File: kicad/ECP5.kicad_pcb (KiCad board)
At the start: 4 copper layers, 64.4 x 54.6 mm, 28 parts, among them J1 FLE-126-01-G-DV, SW1 PTS645SK43SMTR92 LFS

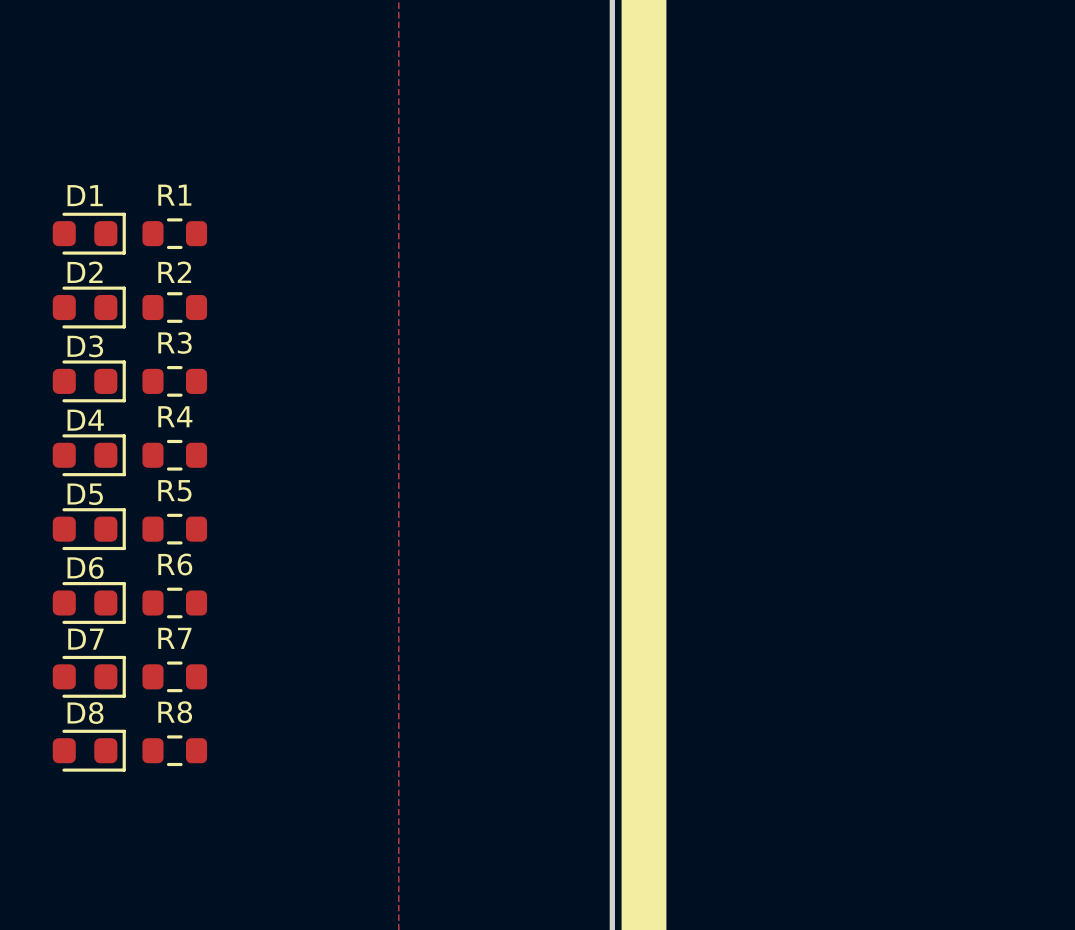
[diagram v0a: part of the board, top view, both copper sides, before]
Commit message: Changed the name of the project path to ECP5_BGA381_FT2232HQ_FIFO_EXT
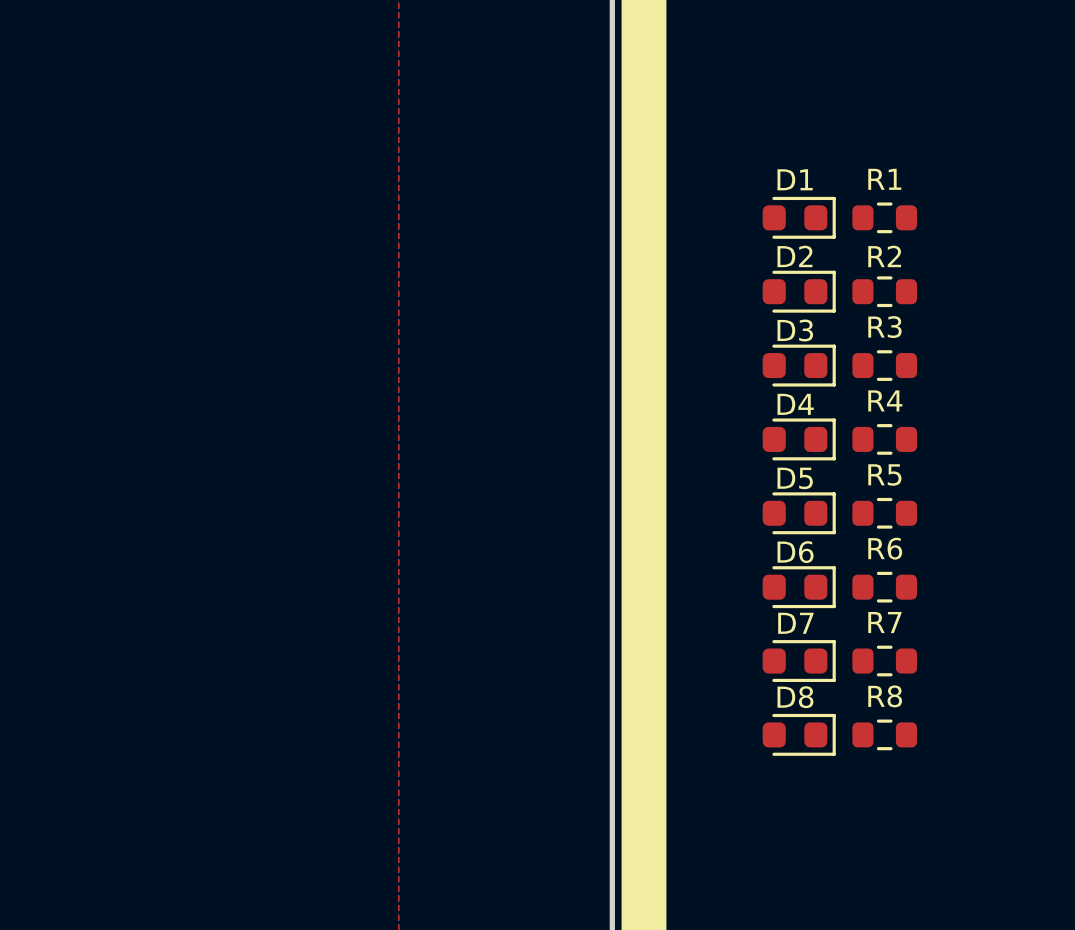
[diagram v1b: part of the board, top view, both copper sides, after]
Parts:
- J1: footprint ECP5_TX_AUDIO_EXT:SAMTEC_FLE-126-01-G-DV -> ECP5_BGA381_FT2232HQ_FIFO_EXT:SAMTEC_FLE-126-01-G-DV
- TP1, TP2, TP3, TP4, TP5: footprint ECP5_TX_AUDIO_EXT:KEYSTONE_5197TR -> ECP5_BGA381_FT2232HQ_FIFO_EXT:KEYSTONE_5197TR
- moved R1 26.9 mm to (127.3, 85.4)
- moved R2 26.9 mm to (127.3, 88.2)
- moved R3 26.9 mm to (127.3, 91.0)
- moved R4 26.9 mm to (127.3, 93.8)
- moved R5 26.9 mm to (127.3, 96.6)
- moved R6 26.9 mm to (127.3, 99.4)
- moved R7 26.9 mm to (127.3, 102.2)
- moved R8 26.9 mm to (127.3, 105.0)
- moved D1 26.9 mm to (123.9, 85.4)
- moved D2 26.9 mm to (123.9, 88.2)
- moved D3 26.9 mm to (123.9, 91.0)
- moved D4 26.9 mm to (123.9, 93.8)
- moved D5 26.9 mm to (123.9, 96.6)
- moved D6 26.9 mm to (123.9, 99.4)
- moved D7 26.9 mm to (123.9, 102.2)
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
